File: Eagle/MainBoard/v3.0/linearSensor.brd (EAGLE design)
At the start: 30.5 x 21.8 mm, 15 parts, among them X1 FH12-08S-1SH

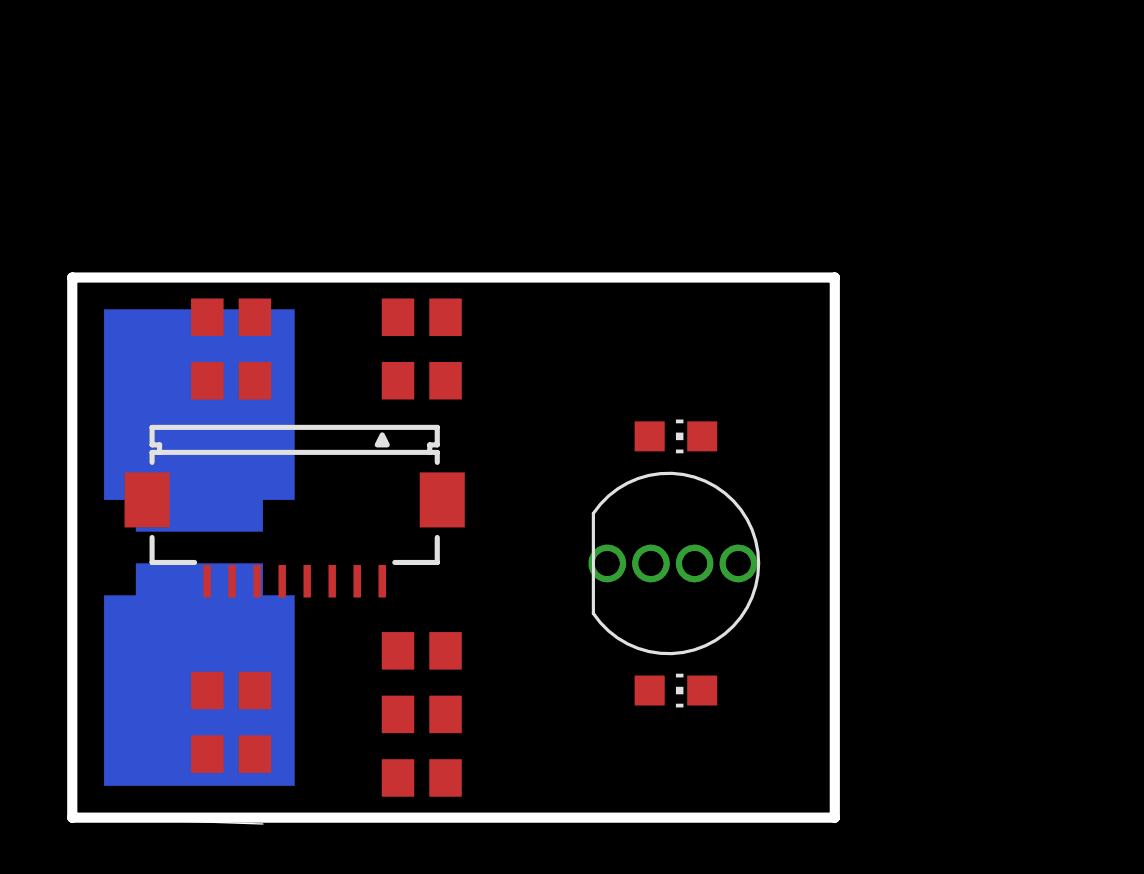
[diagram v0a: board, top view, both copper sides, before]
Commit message: New spectrophotometer board
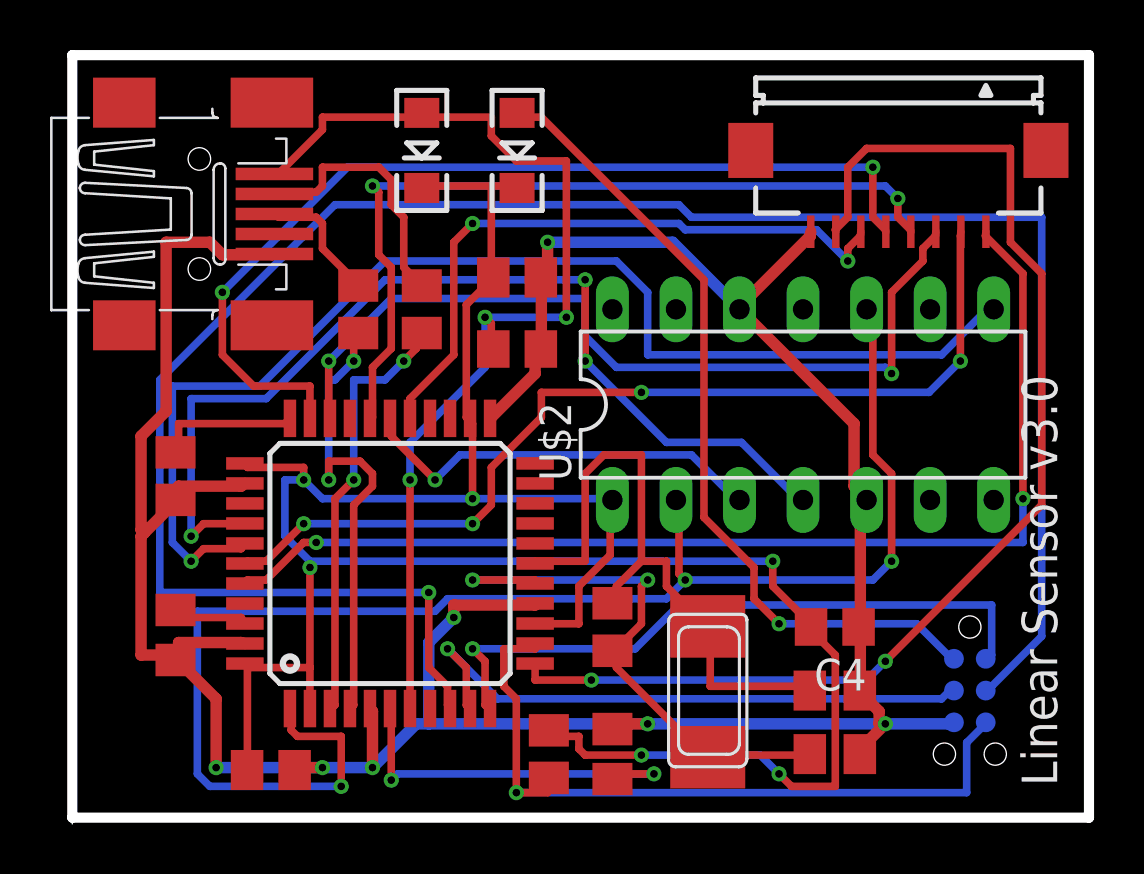
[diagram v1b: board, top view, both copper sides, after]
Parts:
- removed C1: 100pF, rcl:C0805
- removed LED1, LED5: WHITE, led:CHIP-LED0805
- removed PAD1, PAD2: (no value), wirepad:SMD2,54-5,08
- removed RL1, RL7: 1M, rcl:R0805
- removed RL2, RL4: 150, rcl:R0805
- removed RL3, RL5, RL6: 100, rcl:R0805
- removed U$1: RGB-COMMON-CATHODE, lpatiny:LED-TRICOLOR-THROUGHHOLE
- added C10: 10uF, rcl:M0805
- added C11, C3: 100nF, rcl:C0805K
- added C12: 100nF, rcl:M0805
- added C4: 100nF, rcl:C0805
- added C7: 10uF, rcl:C0805
- added C8: 22pF, rcl:C0805K
- added CON1: SPI, lpatiny:TC2030-MCP-NL
- added D2, D4: 1N581, lpatiny:LED-1206
- added R13: 1M, rcl:M0805
- added R15, R3: 10k, resistor:M0805
- added R24, R31: 22, rcl:M0805
- added U$2: TSL1402R, lpatiny:DIL14
- added U$4: 32U4, adafruit:TQFP44
- added X3: 16MHz, lpatiny:NX6035
- added X4: MINI-USB, con-cypressindustries:32005-201
- C2: value 100pF -> 22pF; device rcl:C0805 -> rcl:C0805K
- moved X1 27.9 mm to (33.0, 26.7)
- moved C2 24.1 mm to (30.5, 2.54), turned to 180 degrees
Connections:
- removed net BLUE: RL2.2, X1.4
- removed net GREEN: RL3.2, X1.3
- removed net N$1: RL4.2, U$1.GRN
- removed net N$2: RL3.1, U$1.BLU
- removed net N$3: RL2.1, U$1.RED
- removed net N$4: LED5.A, RL5.1
- removed net N$5: LED1.A, RL6.1
- removed net PULSE: RL1.1, RL7.1, X1.6
- removed net RED: RL4.1, X1.2
- removed net SENS1: C2.1, PAD1.1, RL7.2, X1.7
- removed net SENS2: C1.1, PAD2.1, RL1.2, X1.8
- removed net WHITE: RL5.2, RL6.2, X1.5
- new net +5V/1: C10.2, C12.2, C4.2, D2.C, D4.C, R15.2, U$2.1, U$4.14, U$4.2, U$4.24, U$4.34, U$4.44
- new net A0: U$4.36
- new net A1: U$2.4, U$4.37
- new net A2: U$2.8, U$4.38
- new net A3: U$4.39, X1.2
- new net A4: U$4.40, X1.1
- new net A5: U$4.41
- new net AREF: C11.1, U$4.42
- new net CS: U$4.25
- new net D+USB: R24.2, X4.3
- new net D-USB: R31.2, X4.2
- new net D10*: U$4.30
- new net D11*: U$4.12, X1.7
- new net D12*: U$4.26
- new net D13*: U$4.32, X1.5
- new net D5*: U$4.31, X1.3
- new net D6*: U$4.27, X1.6
- new net D7*: U$2.10, U$2.2, U$4.1
- new net D8*: U$2.3, U$4.28
- new net D9*: U$4.29, X1.4
- new net HWB: R3.2, U$4.33
- new net ISP+5V: CON1.5V, D2.A
- new net MISO: CON1.MISO, U$4.11
- new net MOSI: CON1.MOSI, U$4.10
- new net N$16: C3.2, U$4.6
- new net N$42: C8.2, R13.2, U$4.17, X3.P$2
- new net RD+: R24.1, U$4.4
- new net RD-: R31.1, U$4.3
- new net RESET: CON1.RESET, R15.1, U$4.13
- new net RX: U$4.20
- new net RXLED: U$4.8
- new net SCK: CON1.SCK, U$4.9
- new net SCL: U$4.18
- new net SDA: U$4.19
- new net TX: U$4.21
- new net TXLED: U$4.22
- new net VUSB: C7.2, D4.A, U$4.7, X4.1
- new net XTAL1: C2.2, R13.1, U$4.16, X3.P$1
- net GND: now also C10.1, C11.2, C12.1, C2.1, C3.1, C4.1, C7.1, C8.1, CON1.GND, R3.1, U$2.12, U$2.5, U$4.15, U$4.23, U$4.35, U$4.43, U$4.5, X1.8, X4.5; no longer C1.2, C2.2, LED1.C, LED5.C, U$1.GND, X1.1
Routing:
- net GND: track 0.00 -> 122.4 mm, vias 0 -> 7
- net +5V/1: track 0.00 -> 98.2 mm, vias 0 -> 6
- net SCK: track 0.00 -> 82.5 mm, vias 0 -> 1
- net D7*: track 0.00 -> 59.8 mm, vias 0 -> 3
- net A2: track 0.00 -> 48.4 mm, vias 0 -> 1
- net D11*: track 0.00 -> 48.2 mm, vias 0 -> 2
- net A4: track 0.00 -> 44.8 mm, vias 0 -> 2
- net VUSB: track 0.00 -> 42.1 mm, vias 0 -> 3
- net A1: track 0.00 -> 39.8 mm, vias 0 -> 3
- net D13*: track 0.00 -> 38.7 mm, vias 0 -> 2
- net A3: track 0.00 -> 38.6 mm, vias 0 -> 4
- net D5*: track 0.00 -> 34.4 mm, vias 0 -> 2
- net ISP+5V: track 0.00 -> 32.8 mm, vias 0 -> 1
- net D9*: track 0.00 -> 32.7 mm, vias 0 -> 2
- net RESET: track 0.00 -> 30.4 mm, vias 0 -> 1
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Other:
- board size 30.5 x 21.8 mm -> 40.6 x 30.7 mm
- board text added: "Linear Sensor v3.0"
